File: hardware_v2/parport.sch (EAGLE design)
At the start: 5 parts, among them K1 PIN20X2, U1 SN74LVC161284DL

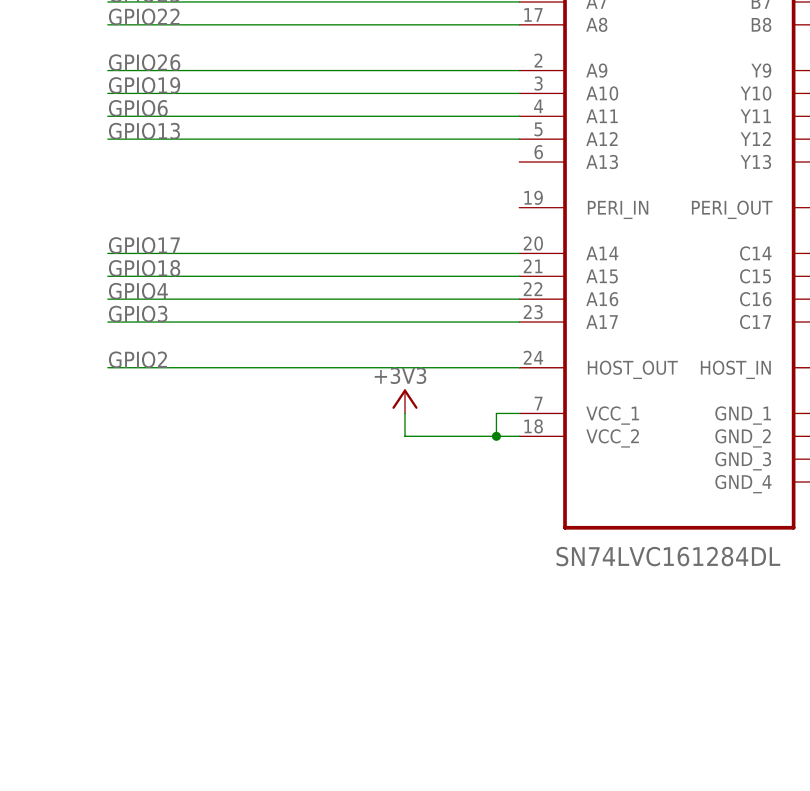
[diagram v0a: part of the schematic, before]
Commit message: hardware_v2: fix drc errors, add silk title
This version ordered from OSH Park (3 boards).
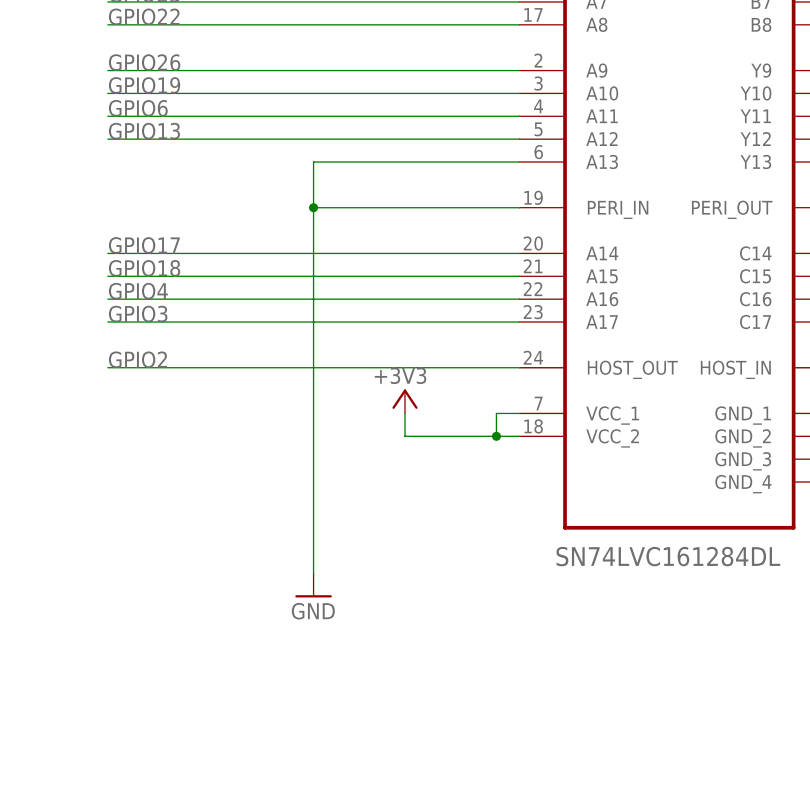
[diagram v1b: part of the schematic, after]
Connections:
- net GND: now also U1.A13, U1.PERI_IN
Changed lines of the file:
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@@
 <part name="R1" library="resistor" deviceset="R-EU_" device="R0805" value="1.4K"/>
 <part name="P+2" library="supply1" deviceset="+5V" device=""/>
+<part name="GND4" library="supply1" deviceset="GND" device=""/>
 </parts>
 <sheets>
@@
 <attribute name="VALUE" x="251.46" y="127" size="1.778" layer="96" rot="R180"/>
 </instance>
+<instance part="GND4" gate="1" x="160.02" y="104.14"/>
 </instances>
 <busses>
@@
 <wire x1="73.66" y1="38.1" x2="73.66" y2="35.56" width="0.1524" layer="91"/>
 </segment>
+<segment>
+<pinref part="U1" gate="A" pin="PERI_IN"/>
+<pinref part="GND4" gate="1" pin="GND"/>
+<wire x1="182.88" y1="147.32" x2="160.02" y2="147.32" width="0.1524" layer="91"/>
+<wire x1="160.02" y1="147.32" x2="160.02" y2="106.68" width="0.1524" layer="91"/>
+<pinref part="U1" gate="A" pin="A13"/>
+<wire x1="182.88" y1="152.4" x2="160.02" y2="152.4" width="0.1524" layer="91"/>
+<wire x1="160.02" y1="152.4" x2="160.02" y2="147.32" width="0.1524" layer="91"/>
+<junction x="160.02" y="147.32"/>
+</segment>
 </net>
